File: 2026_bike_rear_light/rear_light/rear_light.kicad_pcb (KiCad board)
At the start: 2 copper layers, 17 parts, among them J1 Conn_01x04, J2 Conn_01x05, Q1 2N5551, Q2 FQP27P06, Q4 FQP27P06, Q5 2N5551, Q6 2N5551, U1 LM2596HV

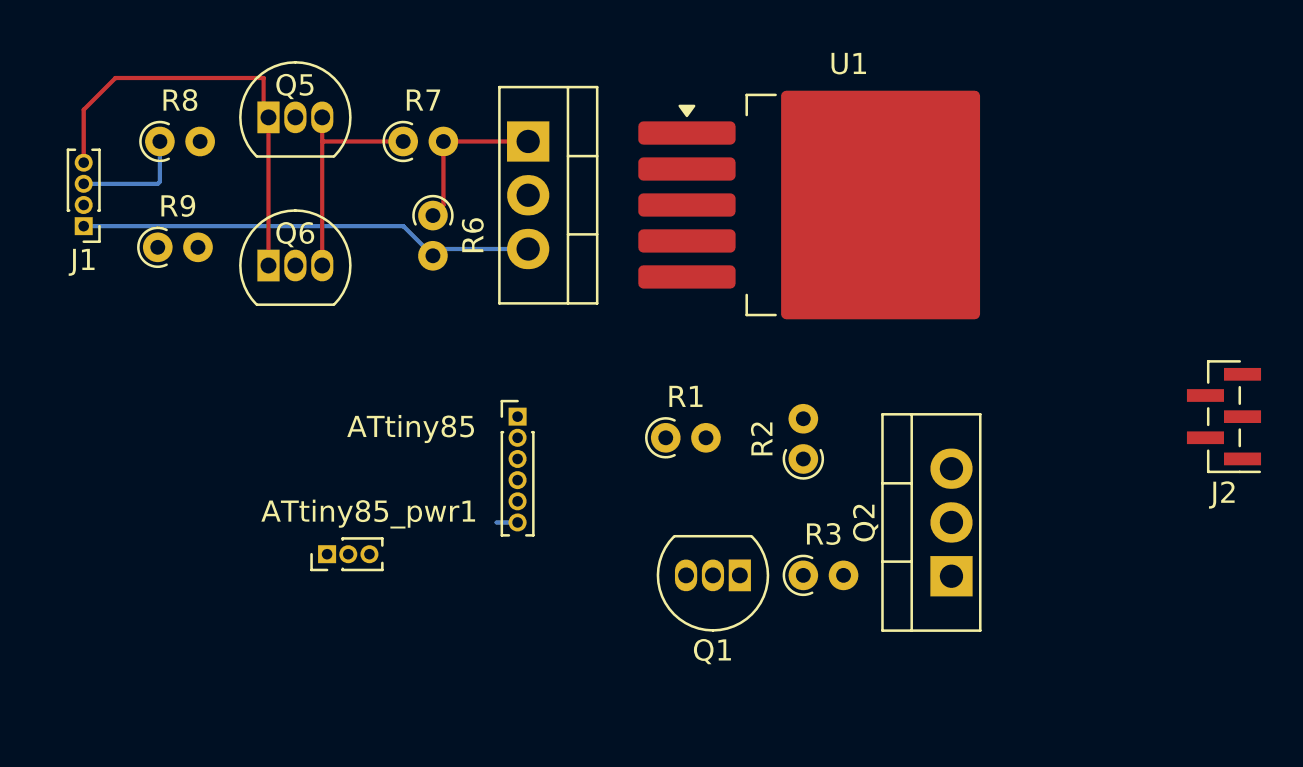
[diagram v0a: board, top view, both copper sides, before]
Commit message: Rear Bike Light - Update schematic and PBC layout  - Remove the older brake light circuit  - Layout the PCB components (roughly)
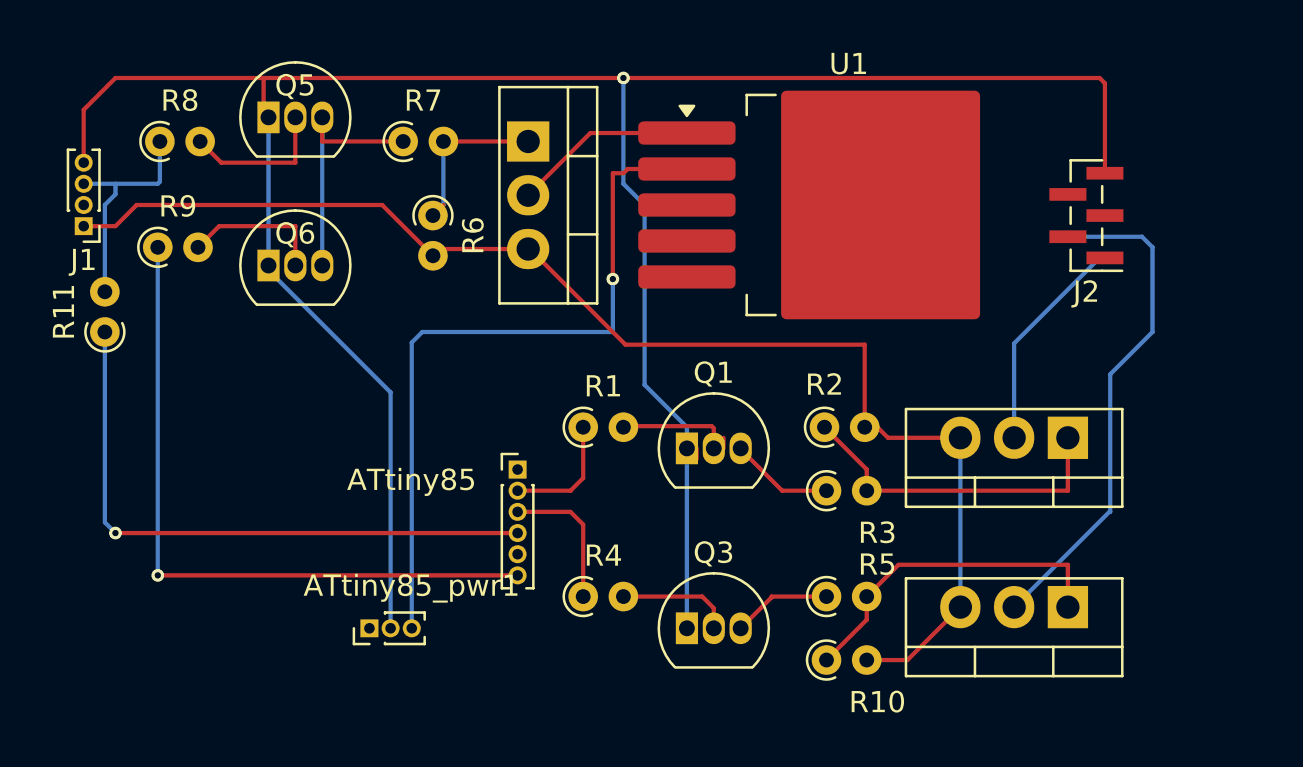
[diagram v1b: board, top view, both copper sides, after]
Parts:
- added Q3: 2N5551, Package_TO_SOT_THT:TO-92_Inline, F.Cu at (189.0, 136.0)
- added Q7: FQP27P06, Package_TO_SOT_THT:TO-220-3_Vertical, F.Cu at (207.0, 135.0)
- added R10: 10k, Resistor_THT:R_Axial_DIN0204_L3.6mm_D1.6mm_P1.90mm_Vertical, F.Cu at (195.6, 137.5)
- added R11: 10k, Resistor_THT:R_Axial_DIN0204_L3.6mm_D1.6mm_P1.90mm_Vertical, F.Cu at (161.5, 122.0)
- added R4: 33k, Resistor_THT:R_Axial_DIN0204_L3.6mm_D1.6mm_P1.90mm_Vertical, F.Cu at (184.1, 134.5)
- added R5: 33k, Resistor_THT:R_Axial_DIN0204_L3.6mm_D1.6mm_P1.90mm_Vertical, F.Cu at (195.6, 134.5)
- moved J2 11.5 mm to (207.9, 116.5)
- moved Q2 8.55 mm to (207.0, 127.0), turned to 180 degrees
- moved Q1 6.50 mm to (189.0, 127.5), turned to 0 degrees
- moved R3 4.15 mm to (195.6, 129.5)
- moved ATtiny85_pwr1 4.03 mm to (174.0, 136.0)
- moved R1 3.93 mm to (184.1, 126.5)
- moved ATtiny85 2.50 mm to (181.0, 128.5)
- moved R2 1.80 mm to (195.5, 126.5), turned to 0 degrees
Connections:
- ATtiny85 pad 4: +5V -> /PB3
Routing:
- net GND: track 20.6 -> 112.0 mm, vias 0 -> 1
- net +48V: track 21.8 -> 63.0 mm
- net VIN: track 0.00 -> 34.3 mm, vias 0 -> 1
- net /PB5: track 1.00 -> 32.5 mm, vias 0 -> 1
- net /PB3: track 0.00 -> 28.7 mm, vias 0 -> 1
- net /BRAKE: track 0.00 -> 23.9 mm
- net Net-(Q7-G): track 0.00 -> 15.9 mm
- net Net-(Q2-G): track 0.00 -> 15.8 mm
- net /TAIL: track 0.00 -> 10.2 mm
- net Net-(Q4-D): track 0.00 -> 8.72 mm
- net Net-(Q5-B): track 0.00 -> 7.05 mm
- net Net-(Q6-B): track 0.00 -> 6.87 mm
- net /BRAKE_LIGHT: track 0.00 -> 6.75 mm
- net Net-(Q1-B): track 0.00 -> 5.78 mm
- net /PB1: track 0.00 -> 5.75 mm
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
